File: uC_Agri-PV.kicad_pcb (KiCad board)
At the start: 4 copper layers, 113 x 113 mm, 248 parts, among them IC1 ESDALC6V1W5, IC2 DMP1045U-7, IC201 ESDALC6V1W5, IC202 ESDALC6V1W5, IC203 ESDALC6V1W5, IC601 MMS9013-L-TP, IC602 MMS9013-L-TP, IC701 TPS63021DSJR, IC8 317990687, J1 PJ-102B, J4 USB_B_Micro, J502 503398-1892, J6 Conn_Coaxial, J601 USB_B_Micro, Q1 IRLML6402, Q2 IRLML6402, Q201 DMG1012T-13, Q202 DMG1012T-13, Q203 DMG1012T-13, Q204 DMG1012T-13, Q501 IRLML6402, Q7 IRLML6402, Q701 IRLML6402, Q8 IRLML6402, Q801 IRLML6402, Q802 IRLML6402, Q803 IRLML6402, Q804 IRLML6402, Q805 IRLML6402, SW1 SW_SPDT, SW2 SW_DIP_x01, SW3 SW_DIP_x01, U201 TLV9304IDR, U202 STM32U575ZIT6Q, U3 ESP32-C6-WROOM-1-N8, U4 AMS1117-3.3, U702 TLV9304IDR, U801 TPS61023DRLR, U802 ISL83078EIBZA, X1 Conn_01x06_Pin, X10 Conn_02x02_Counter_Clockwise, X11 Conn_01x04_Pin, X12 Conn_01x04_Pin, X13 Conn_01x07_Pin, X14 Conn_01x03_Pin, X15 Conn_01x03_Pin, X16 Conn_01x03_Pin, X17 Conn_01x03_Pin, X18 Conn_01x04_Pin, X19 Conn_01x05_Pin, X2 Conn_01x06_Pin, X20 3220-10-0100-00, X21 Conn_01x02_Pin, X22 Conn_01x02_Pin, X3 Conn_01x04_Pin, X4 Conn_01x04_Pin, X5 Conn_01x07_Pin, X6 Conn_01x06_Pin, X601 XTAL_4_PINS, X602 XTAL_2_PINS, X7 Conn_01x04_Pin, X8 Conn_01x04_Pin, X9 Conn_01x04_Pin

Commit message: Zwei falsche Vias (Achtung Kurzschluss) entfernt und Beschriftung STM-UART Stiftleisten und USB-Anschlüsse angepasst
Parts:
- moved C4 0.51 mm to (83.4, 44.1)
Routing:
- net GND: track 161.9 -> 157.8 mm
- net (no net): vias 2 -> 0
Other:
- board text added: "ESP USB"
- board text added: "STM USB"
- board text added: "UART"
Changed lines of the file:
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@@
 	(footprint "Capacitor_SMD:C_0805_2012Metric_Pad1.18x1.45mm_HandSolder"
 		(layer "F.Cu")
-		(at 83.425 43.595)
+		(at 83.4 44.1)
 		(descr "Capacitor SMD 0805 (2012 Metric), square (rectangular) end terminal, IPC_7351 nominal with elongated pad for handsoldering. (Body size source: IPC-SM-782 page 76, https://www.pcb-3d.com/wordpress/wp-content/uploads/ipc-sm-782a_amendment_1_and_2.pdf, https://docs.google.com/spreadsheets/d/1BsfQQcO9C6DZCsRaXUlFlo91Tg2WpOkGARC1WS5S8t0/edit?usp=sharing), generated with kicad-footprint-generator")
 		(tags "capacitor handsolder")
 		(property "Reference" "C4"
-			(at -2.95 1.15 0)
+			(at -3.1 0.6 0)
 			(layer "F.SilkS")
 			(effects
@@
 		(tags "resistor handsolder")
 		(property "Reference" "R612"
-			(at 0.95 1.75 0)
+			(at -4.003 -0.003 0)
 			(layer "F.SilkS")
 			(effects
@@
 		)
 		(property "Value" "330k"
-			(at 0 1.65 0)
+			(at -0.003 1.697 0)
 			(layer "F.Fab")
 			(effects
@@
 		)
 	)
+	(gr_text "ESP USB"
+		(at 81.8 42.7 0)
+		(layer "F.SilkS")
+		(effects
+			(font
+				(size 1 1)
+				(thickness 0.2)
+				(bold yes)
+			)
+			(justify left bottom)
+		)
+	)
 	(gr_text "PAR_Sensor"
 		(at 22 136.3 0)
@@
 		)
 	)
-	(gr_text "GPIO STM"
-		(at 44.6 96.4 0)
+	(gr_text "UART"
+		(at 46.1 96.5 0)
 		(layer "F.SilkS")
 		(effects
@@
 		)
 	)
+	(gr_text "STM USB"
+		(at 124 95.4 90)
+		(layer "F.SilkS")
+		(effects
+			(font
+				(size 1 1)
+				(thickness 0.2)
+				(bold yes)
+			)
+			(justify left bottom)
+		)
+	)
 	(gr_text "OneWire 1/2"
 		(at 19.3 96.8 0)
@@
 		)
 	)
-	(via
-		(at 33 75)
-		(size 2)
-		(drill 1.8)
-		(layers "F.Cu" "B.Cu")
-		(free yes)
-		(net 0)
-	)
-	(via
-		(at 124.1 36.8)
-		(size 0.6)
-		(drill 0.3)
-		(layers "F.Cu" "B.Cu")
-		(net 0)
-	)
 	(segment
 		(start 75.15 124.9)
@@
 	)
 	(segment
+		(start 82.3875 44.1)
+		(end 81.33 44.1)
+		(width 0.5)
+		(layer "F.Cu")
+		(net 5)
+	)
+	(segment
 		(start 68.05 40.2)
 		(end 67.65 39.8)
@@
 	)
 	(segment
-		(start 83.7 39.89)
-		(end 83.7 42.2825)
-		(width 0.5)
-		(layer "F.Cu")
-		(net 5)
-	)
-	(segment
 		(start 68.9 101.9)
 		(end 69.3125 101.4875)
@@
 	)
 	(segment
-		(start 80.925 43.595)
-		(end 80.875 43.645)
-		(width 0.5)
-		(layer "F.Cu")
-		(net 5)
-	)
-	(segment
 		(start 76.7 53.9375)
 		(end 76.7 55.55)
@@
 	)
 	(segment
-		(start 82.3875 43.595)
-		(end 80.925 43.595)
-		(width 0.5)
-		(layer "F.Cu")
-		(net 5)
-	)
-	(segment
 		(start 117.4125 42.4)
 		(end 118.2125 43.2)
@@
 	)
 	(segment
+		(start 81.33 44.1)
+		(end 80.875 43.645)
+		(width 0.5)
+		(layer "F.Cu")
+		(net 5)
+	)
+	(segment
 		(start 89.6 105.8875)
 		(end 88.4375 107.05)
@@
 	)
 	(segment
-		(start 83.7 42.2825)
-		(end 82.3875 43.595)
-		(width 0.5)
-		(layer "F.Cu")
-		(net 5)
-	)
-	(segment
 		(start 128.332 91.067)
 		(end 128.332 89.567)
@@
 	)
 	(segment
-		(start 84.4625 43.595)
-		(end 85.775 43.595)
-		(width 0.3)
-		(layer "F.Cu")
-		(net 16)
-	)
-	(segment
 		(start 87.465 43.8)
 		(end 87.42 43.845)
@@
 	)
 	(segment
-		(start 85.775 43.595)
-		(end 86.4725 42.8975)
-		(width 0.3)
-		(layer "F.Cu")
-		(net 16)
-	)
-	(segment
 		(start 85 39.89)
 		(end 85.025 39.865)
@@
 	)
 	(segment
+		(start 85.27 44.1)
+		(end 86.4725 42.8975)
+		(width 0.3)
+		(layer "F.Cu")
+		(net 16)
+	)
+	(segment
 		(start 87.425 43.85)
 		(end 87.425 44.945)
@@
 		(width 0.3)
 		(layer "F.Cu")
+		(net 16)
+	)
+	(segment
+		(start 84.4625 44.1)
+		(end 85.27 44.1)
+		(width 0.3)
+		(layer "F.Cu")

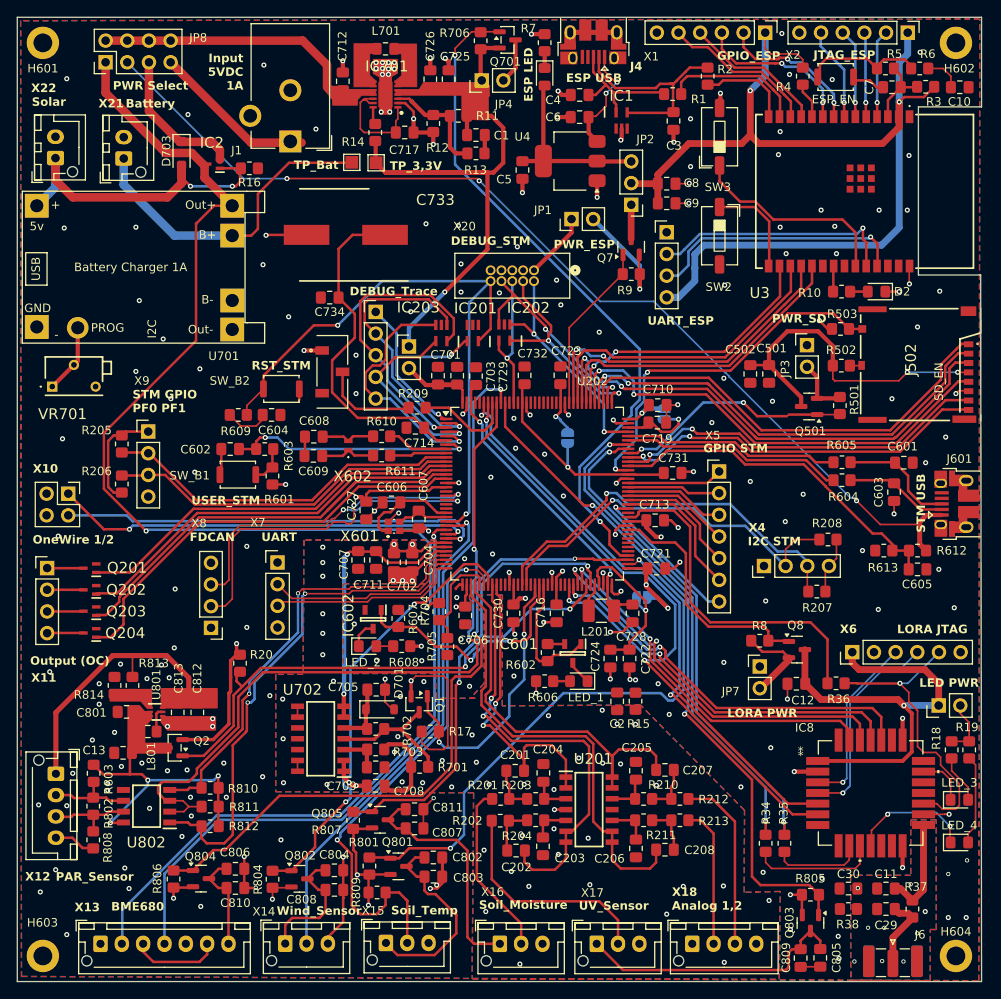
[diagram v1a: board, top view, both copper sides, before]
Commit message: Änderung Beschriftungen und Drehung X8 (3V3 gleich zu X7)
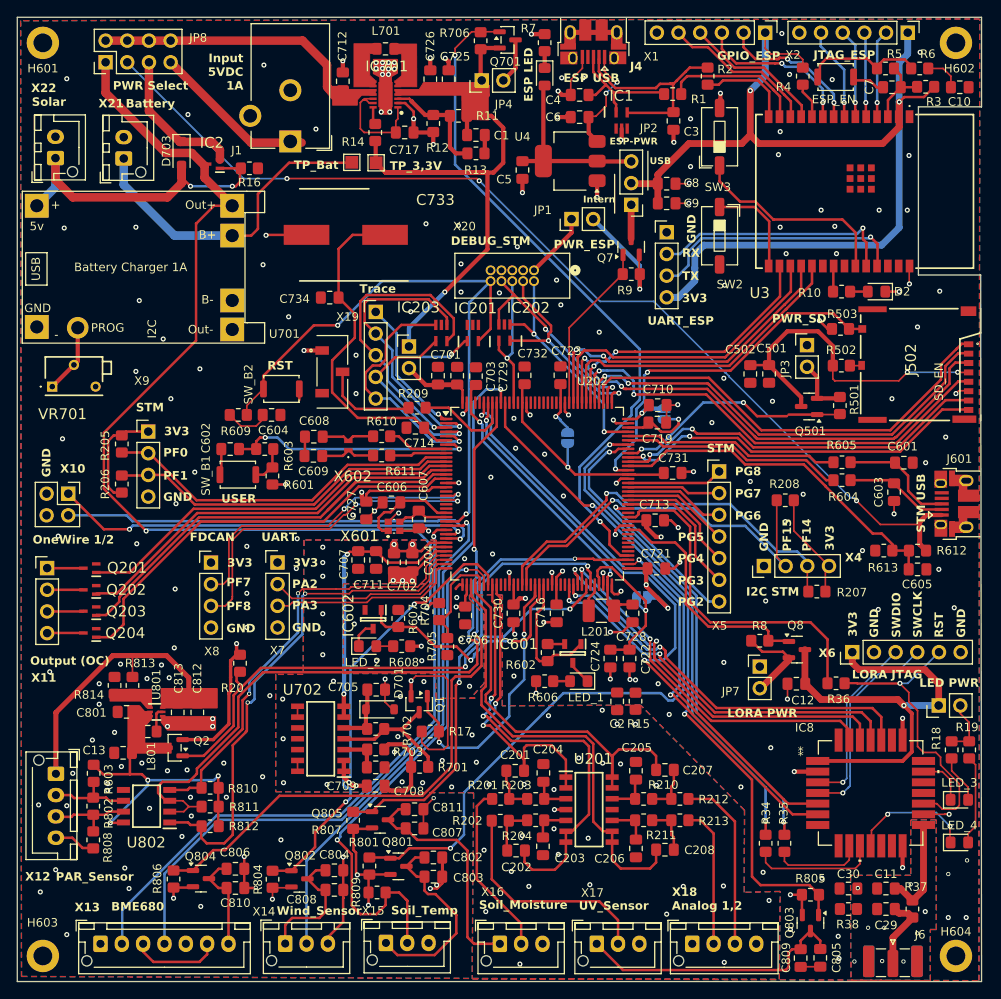
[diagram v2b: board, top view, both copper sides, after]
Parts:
- moved X8 7.65 mm to (40.2, 98.9), turned to 0 degrees
- moved R208 6.79 mm to (107.5, 91.6)
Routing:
- net +3.3V: track 104.5 -> 110.4 mm
- net GND: track 157.8 -> 162.9 mm, vias 198 -> 206
- net Net-(U202-PF7): track 41.3 -> 37.6 mm
- net Net-(U202-PF8): track 37.4 -> 39.4 mm
- net Net-(U202-PF15): track 45.2 -> 46.9 mm
- net /Power Supply/Vdd_MCU: track 162.4 -> 161.4 mm
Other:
- board text added: "3V3"
- board text added: "ESP-PWR"
- board text added: "GND"
- board text added: "Intern"
- board text added: "PA2"
- board text added: "PA3"
- board text added: "PF0"
- board text added: "PF1"
- board text added: "PF14"
- board text added: "PF15"
- board text added: "PF7"
- board text added: "PF8"
- board text added: "PG2"
- board text added: "PG3"
- board text added: "PG4"
- board text added: "PG5"
- board text added: "PG6"
- board text added: "PG7"
- board text added: "PG8"
- board text added: "RST"
- board text added: "RX"
- board text added: "STM"
- board text added: "SWCLK"
- board text added: "SWDIO"
- board text added: "TX"
- board text added: "Trace"
- board text added: "USB"
- board text added: "USER"
- board text removed: "DEBUG_Trace"
- board text removed: "GPIO STM"
- board text removed: "RST_STM"
- board text removed: "STM GPIO PF0 PF1"
- board text removed: "USER_STM"
